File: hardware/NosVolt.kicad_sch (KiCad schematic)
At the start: 15 parts, among them J101 INPUTS, J102 OUTPUTS, SW101 SW_Reset, SW102 SSSS811101, U102 GMT028-05, U103 ESP32-C3-MINI-1

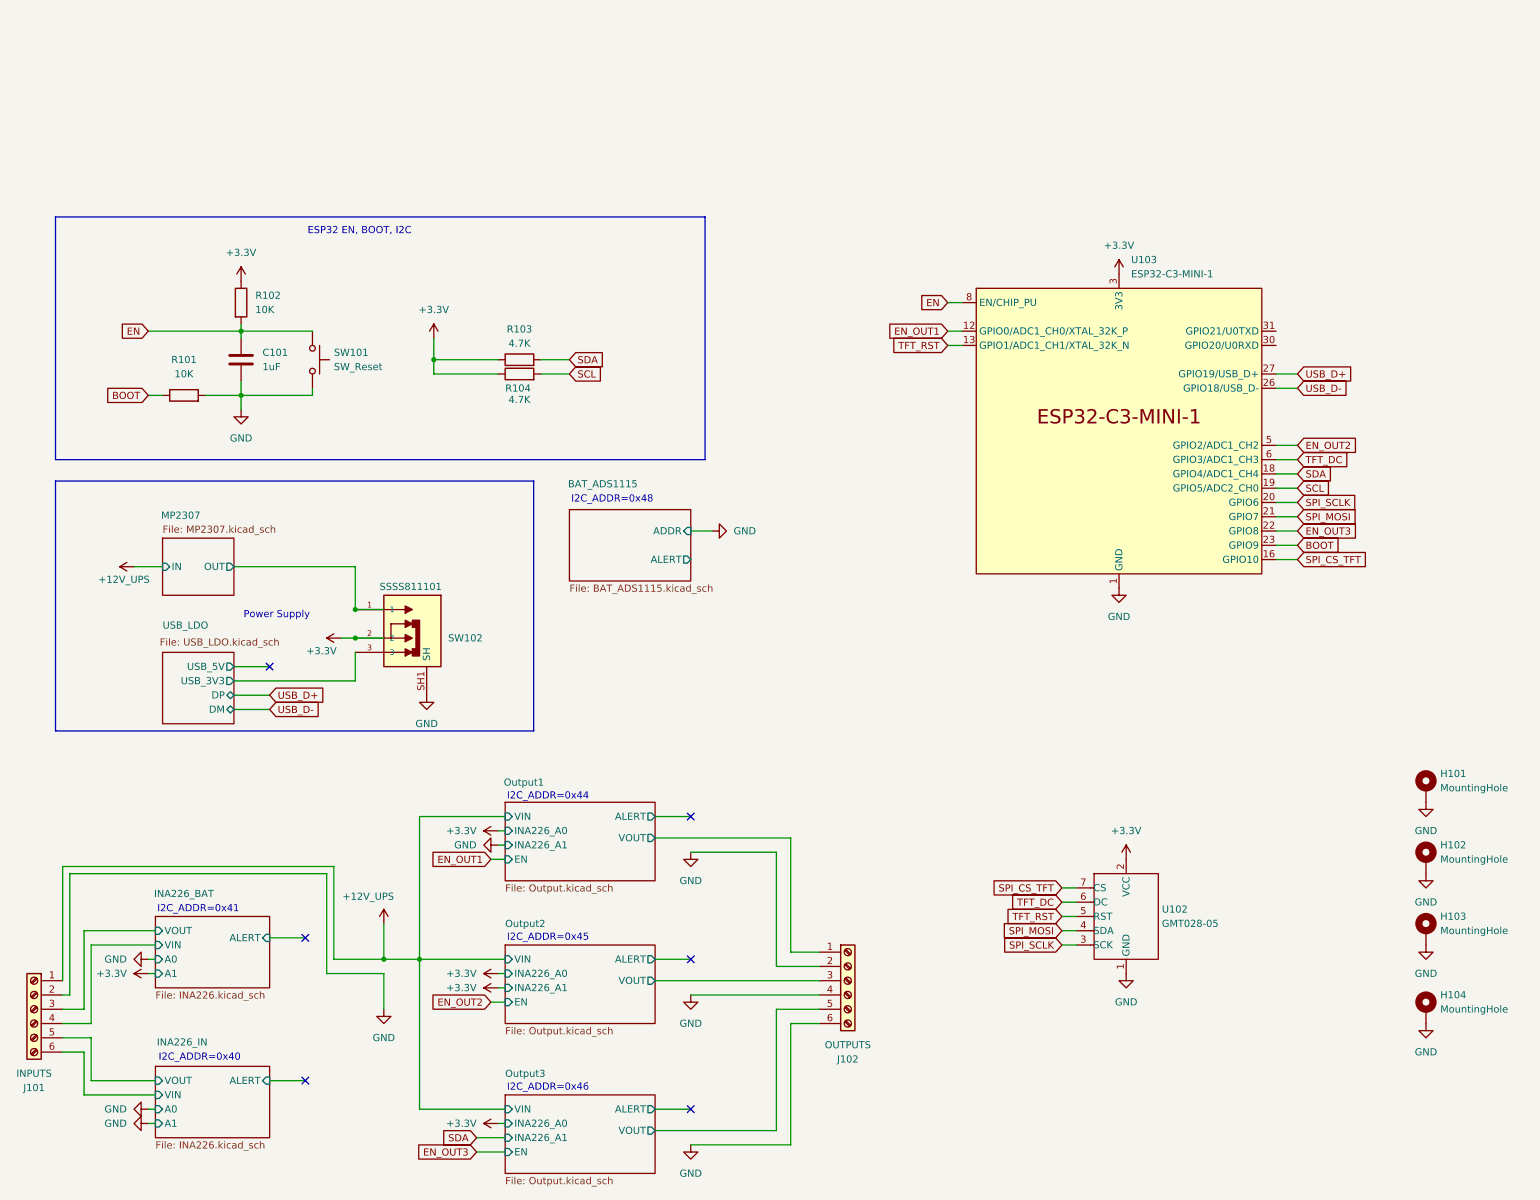
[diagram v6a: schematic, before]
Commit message: thermal relief
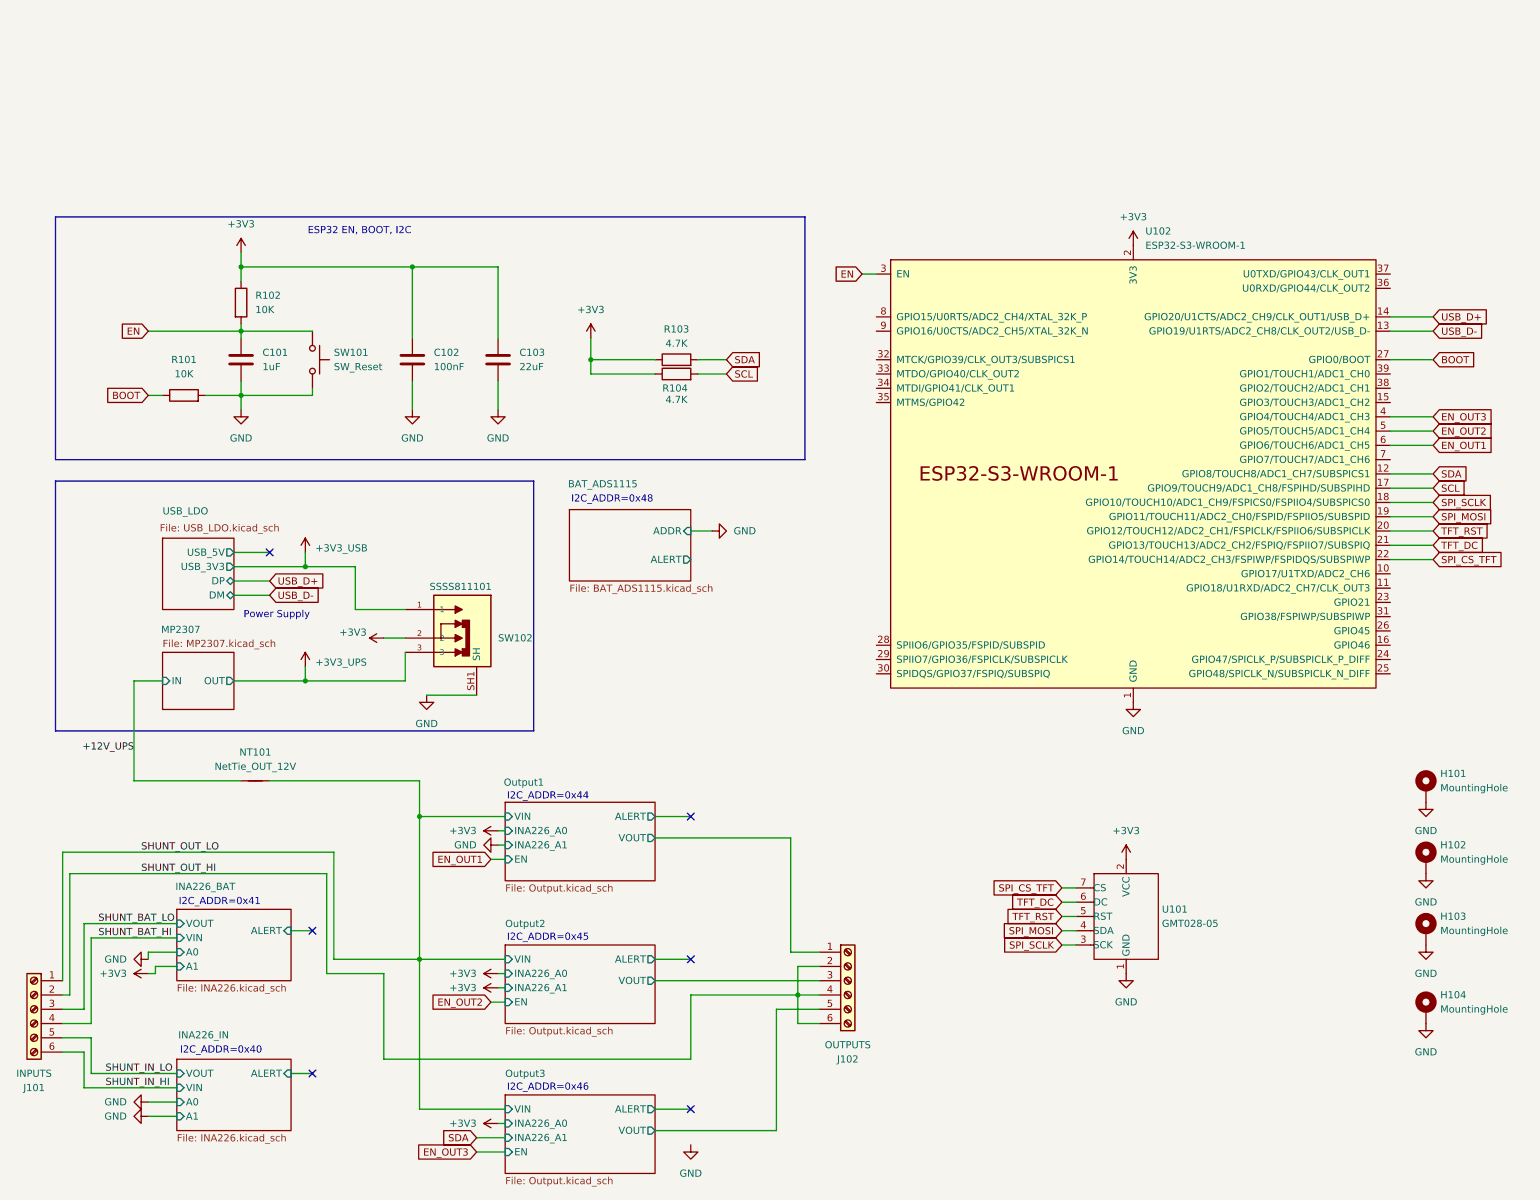
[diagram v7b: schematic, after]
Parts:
- removed U103: ESP32-C3-MINI-1, PCM_Espressif:ESP32-C3-MINI-1, symbol PCM_Espressif:ESP32-C3-MINI-1
- added C102: 100nF, Capacitor_SMD:C_0603_1608Metric, symbol Device:C
- added C103: 22uF, Capacitor_SMD:C_0805_2012Metric, symbol Device:C
- added NT101: NetTie_OUT_12V, NetTie:NetTie-2_SMD_Pad0.5mm, symbol Device:NetTie_2
- added U102: ESP32-S3-WROOM-1, PCM_Espressif:ESP32-S3-WROOM-1, symbol PCM_Espressif:ESP32-S3-WROOM-1
- H101, H102, H103, H104: footprint MountingHole_3.2mm_M3_Pad_Via -> MountingHole:MountingHole_3.2mm_M3_Pad_Via
- renumbered U102 to U101
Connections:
- net +12V_UPS: now also NT101.1; no longer J101.1 (Pin_1)
- net BOOT: now also U102.27 (GPIO0/BOOT)
- net EN: now also U102.3 (EN)
- net EN_OUT1: now also U102.6 (GPIO6/TOUCH6/ADC1_CH5)
- net EN_OUT2: now also U102.5 (GPIO5/TOUCH5/ADC1_CH4)
- net EN_OUT3: now also U102.4 (GPIO4/TOUCH4/ADC1_CH3)
- net GND: now also C102.2, C103.2, U102.1 (GND), U102.40 (GND), U102.41 (GND); no longer J101.2 (Pin_2), J102.2 (Pin_2), J102.4 (Pin_4), J102.6 (Pin_6)
- net SCL: now also U102.17 (GPIO9/TOUCH9/ADC1_CH8/FSPIHD/SUBSPIHD)
- net SDA: now also U102.12 (GPIO8/TOUCH8/ADC1_CH7/SUBSPICS1)
- net SPI_CS_TFT: now also U102.22 (GPIO14/TOUCH14/ADC2_CH3/FSPIWP/FSPIDQS/SUBSPIWP)
- net SPI_MOSI: now also U102.19 (GPIO11/TOUCH11/ADC2_CH0/FSPID/FSPIIO5/SUBSPID)
- net SPI_SCLK: now also U102.18 (GPIO10/TOUCH10/ADC1_CH9/FSPICS0/FSPIIO4/SUBSPICS0)
- net TFT_DC: now also U102.21 (GPIO13/TOUCH13/ADC2_CH2/FSPIQ/FSPIIO7/SUBSPIQ)
- net TFT_RST: now also U102.20 (GPIO12/TOUCH12/ADC2_CH1/FSPICLK/FSPIIO6/SUBSPICLK)
- net USB_D+: now also U102.14 (GPIO20/U1CTS/ADC2_CH9/CLK_OUT1/USB_D+)
- net USB_D-: now also U102.13 (GPIO19/U1RTS/ADC2_CH8/CLK_OUT2/USB_D-)
- net +3.3V renamed +3V3
- net +3V3: now also C102.1, C103.1, U102.2 (3V3)
- net INA226_BAT/VIN renamed SHUNT_BAT_HI
- net INA226_BAT/VOUT renamed SHUNT_BAT_LO
- net INA226_IN/VIN renamed SHUNT_IN_HI
- net INA226_IN/VOUT renamed SHUNT_IN_LO
- net MP2307/OUT renamed +3V3_USB
- net USB_LDO/USB_3V3 renamed +3V3_UPS
- new net SHUNT_OUT_HI: J101.2 (Pin_2), J102.2 (Pin_2), J102.4 (Pin_4), J102.6 (Pin_6)
- new net SHUNT_OUT_LO: J101.1 (Pin_1), NT101.2
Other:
- moved on the sheet: R103, R104, SW102

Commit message: tracing
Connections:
- net EN_OUT1: now also U102.4 (GPIO4/TOUCH4/ADC1_CH3); no longer U102.6 (GPIO6/TOUCH6/ADC1_CH5)
- net EN_OUT3: now also U102.6 (GPIO6/TOUCH6/ADC1_CH5); no longer U102.4 (GPIO4/TOUCH4/ADC1_CH3)
- net Output1/VOUT renamed SHUNT_OUT_LO1
- net Output2/VOUT renamed SHUNT_OUT_LO2
- net Output3/VOUT renamed SHUNT_OUT_LO3
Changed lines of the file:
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@@
+		)
+	)
+	(label "SHUNT_OUT_LO2"
+		(at 138.43 151.13 0)
+		(effects
+			(font
+				(size 1.27 1.27)
+			)
+			(justify left bottom)
 		)
 	)
@@
 		)
 	)
+	(label "SHUNT_OUT_LO1"
+		(at 154.94 138.43 0)
+		(effects
+			(font
+				(size 1.27 1.27)
+			)
+			(justify left bottom)
+		)
+	)
 	(label "SHUNT_IN_LO"
 		(at 33.02 167.64 0)
@@
 		)
 	)
+	(label "SHUNT_OUT_LO3"
+		(at 152.4 171.45 0)
+		(effects
+			(font
+				(size 1.27 1.27)
+			)
+			(justify left bottom)
+		)
+	)
 	(label "SHUNT_IN_HI"
 		(at 33.02 170.18 0)
@@
 		)
 	)
+	(global_label "EN_OUT3"
+		(shape input)
+		(at 269.24 55.88 0)
+		(fields_autoplaced yes)
+		(effects
+			(font
+				(size 1.27 1.27)
+			)
+			(justify left)
+		)
+		(property "Intersheetrefs" "${INTERSHEET_REFS}"
+			(at 280.5104 55.88 0)
+			(effects
+				(font
+					(size 1.27 1.27)
+				)
+				(justify left)
+				(hide yes)
+			)
+		)
+	)
 	(global_label "USB_D+"
 		(shape input)
@@
 		)
 	)
+	(global_label "SPI_SCLK"
+		(shape input)
+		(at 203.2 144.78 180)
+		(fields_autoplaced yes)
+		(effects
+			(font
+				(size 1.27 1.27)
+			)
+			(justify right)
+		)
+		(property "Intersheetrefs" "${INTERSHEET_REFS}"
+			(at 191.3853 144.78 0)
+			(effects
+				(font
+					(size 1.27 1.27)
+				)
+				(justify right)
+				(hide yes)
+			)
+		)
+	)
+	(global_label "EN_OUT2"
+		(shape input)
+		(at 269.24 53.34 0)
+		(fields_autoplaced yes)
+		(effects
+			(font
+				(size 1.27 1.27)
+			)
+			(justify left)
+		)
+		(property "Intersheetrefs" "${INTERSHEET_REFS}"
+			(at 280.5104 53.34 0)
+			(effects
+				(font
+					(size 1.27 1.27)
+				)
+				(justify left)
+				(hide yes)
+			)
+		)
+	)
+	(global_label "SPI_MOSI"
+		(shape input)
+		(at 269.24 68.58 0)
+		(fields_autoplaced yes)
+		(effects
+			(font
+				(size 1.27 1.27)
+			)
+			(justify left)
+		)
+		(property "Intersheetrefs" "${INTERSHEET_REFS}"
+			(at 280.8733 68.58 0)
+			(effects
+				(font
+					(size 1.27 1.27)
+				)
+				(justify left)
+				(hide yes)
+			)
+		)
+	)
+	(global_label "SDA"
+		(shape input)
+		(at 143.51 40.64 0)
+		(fields_autoplaced yes)
+		(effects
+			(font
+				(size 1.27 1.27)
+			)
+			(justify left)
+		)
+		(property "Intersheetrefs" "${INTERSHEET_REFS}"
+			(at 150.0633 40.64 0)
+			(effects
+				(font
+					(size 1.27 1.27)
+				)
+				(justify left)
+				(hide yes)
+			)
+		)
+	)
+	(global_label "USB_D-"
+		(shape input)
+		(at 62.23 82.55 0)
+		(fields_autoplaced yes)
+		(effects
+			(font
+				(size 1.27 1.27)
+			)
+			(justify left)
+		)
+		(property "Intersheetrefs" "${INTERSHEET_REFS}"
+			(at 72.8352 82.55 0)
+			(effects
+				(font
+					(size 1.27 1.27)
+				)
+				(justify left)
+				(hide yes)
+			)
+		)
+	)
+	(global_label "SPI_SCLK"
+		(shape input)
+		(at 269.24 66.04 0)
+		(fields_autoplaced yes)
+		(effects
+			(font
+				(size 1.27 1.27)
+			)
+			(justify left)
+		)
+		(property "Intersheetrefs" "${INTERSHEET_REFS}"
+			(at 281.0547 66.04 0)
+			(effects
+				(font
+					(size 1.27 1.27)
+				)
+				(justify left)
+				(hide yes)
+			)
+		)
+	)
+	(global_label "BOOT"
+		(shape input)
+		(at 40.64 46.99 180)
+		(fields_autoplaced yes)
+		(effects
+			(font
+				(size 1.27 1.27)
+			)
+			(justify right)
+		)
+		(property "Intersheetrefs" "${INTERSHEET_REFS}"
+			(at 32.7562 46.99 0)
+			(effects
+				(font
+					(size 1.27 1.27)
+				)
+				(justify right)
+				(hide yes)
+			)
+		)
+	)
 	(global_label "EN_OUT1"
 		(shape input)
-		(at 269.24 55.88 0)
-		(fields_autoplaced yes)
-		(effects
-			(font
-				(size 1.27 1.27)
-			)
-			(justify left)
-		)
-		(property "Intersheetrefs" "${INTERSHEET_REFS}"
-			(at 280.5104 55.88 0)
-			(effects
-				(font
-					(size 1.27 1.27)
-				)
-				(justify left)
-				(hide yes)
-			)
-		)
-	)
-	(global_label "SPI_SCLK"
-		(shape input)
-		(at 203.2 144.78 180)
-		(fields_autoplaced yes)
-		(effects
-			(font
-				(size 1.27 1.27)
-			)
-			(justify right)
-		)
-		(property "Intersheetrefs" "${INTERSHEET_REFS}"
-			(at 191.3853 144.78 0)
-			(effects
-				(font
-					(size 1.27 1.27)
-				)
-				(justify right)
-				(hide yes)
-			)
-		)
-	)
-	(global_label "EN_OUT2"
-		(shape input)
-		(at 269.24 53.34 0)
-		(fields_autoplaced yes)
-		(effects
-			(font
-				(size 1.27 1.27)
-			)
-			(justify left)
-		)
-		(property "Intersheetrefs" "${INTERSHEET_REFS}"
-			(at 280.5104 53.34 0)
-			(effects
-				(font
-					(size 1.27 1.27)
-				)
-				(justify left)
-				(hide yes)
-			)
-		)
-	)
-	(global_label "SPI_MOSI"
-		(shape input)
-		(at 269.24 68.58 0)
-		(fields_autoplaced yes)
-		(effects
-			(font
-				(size 1.27 1.27)
-			)
-			(justify left)
-		)
-		(property "Intersheetrefs" "${INTERSHEET_REFS}"
-			(at 280.8733 68.58 0)
-			(effects
-				(font
-					(size 1.27 1.27)
-				)
-				(justify left)
-				(hide yes)
-			)
-		)
-	)
-	(global_label "SDA"
-		(shape input)
-		(at 143.51 40.64 0)
-		(fields_autoplaced yes)
-		(effects
-			(font
-				(size 1.27 1.27)
-			)
-			(justify left)
-		)
-		(property "Intersheetrefs" "${INTERSHEET_REFS}"
-			(at 150.0633 40.64 0)
-			(effects
-				(font
-					(size 1.27 1.27)
-				)
-				(justify left)
-				(hide yes)
-			)
-		)
-	)
-	(global_label "USB_D-"
-		(shape input)
-		(at 62.23 82.55 0)
-		(fields_autoplaced yes)
-		(effects
-			(font
-				(size 1.27 1.27)
-			)
-			(justify left)
-		)
-		(property "Intersheetrefs" "${INTERSHEET_REFS}"
-			(at 72.8352 82.55 0)
-			(effects
-				(font
-					(size 1.27 1.27)
-				)
-				(justify left)
-				(hide yes)
-			)
-		)
-	)
-	(global_label "SPI_SCLK"
-		(shape input)
-		(at 269.24 66.04 0)
-		(fields_autoplaced yes)
-		(effects
-			(font
-				(size 1.27 1.27)
-			)
-			(justify left)
-		)
-		(property "Intersheetrefs" "${INTERSHEET_REFS}"
-			(at 281.0547 66.04 0)
-			(effects
-				(font
-					(size 1.27 1.27)
-				)
-				(justify left)
-				(hide yes)
-			)
-		)
-	)
-	(global_label "BOOT"
-		(shape input)
-		(at 40.64 46.99 180)
-		(fields_autoplaced yes)
-		(effects
-			(font
-				(size 1.27 1.27)
-			)
-			(justify right)
-		)
-		(property "Intersheetrefs" "${INTERSHEET_REFS}"
-			(at 32.7562 46.99 0)
-			(effects
-				(font
-					(size 1.27 1.27)
-				)
-				(justify right)
-				(hide yes)
-			)
-		)
-	)
-	(global_label "EN_OUT3"
-		(shape input)
 		(at 269.24 50.8 0)
